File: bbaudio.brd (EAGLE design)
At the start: 88.9 x 127 mm, 35 parts, among them U1 V_REG_MIC2920, U2 V_REG_MIC2920, U3 LMZ14203

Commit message: Some more tewaks to the power section
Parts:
- removed C3: 1uF, rcl:C0603
- removed C4: 10uF, sparkfun:EIA3216
- removed U1: V_REG_MIC2920, sparkfun:SOT223
- added C10: 10uF, sparkfun:EIA3216
- added C7: 1uF, rcl:C0603
- added U4: VREG, nonolith:SOT23-3
- moved C6 16.1 mm to (62.2, 33.0), turned to 270 degrees
- moved C2 8.52 mm to (43.2, 29.2), turned to 90 degrees
- moved R3 7.73 mm to (67.3, 29.2), turned to 90 degrees
- moved R2 4.58 mm to (50.8, 25.4), turned to 0 degrees
- moved R4 2.84 mm to (64.8, 33.0)
- moved C9 2.84 mm to (64.8, 29.2), turned to 90 degrees
- moved C5 1.27 mm to (47.0, 33.0), turned to 270 degrees
- moved R1 1.27 mm to (50.8, 27.9), turned to 0 degrees
- moved U3 1.27 mm to (54.6, 39.4)
- moved C8 1.27 mm to (55.9, 27.9)
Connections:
- new net VCC: C2.A, U2.3
- net +12V: now also C1.1, U2.1
- net 1.8V: now also C7.1, U4.3; no longer C4.A, U1.3
- net 3.3V: now also C10.A, U4.2; no longer C2.A, C3.1, U1.1, U2.3
- net 5V: no longer C1.1, U2.1
- net GND: now also C10.C, C7.2, U4.1; no longer C3.2, C4.C, U1.2
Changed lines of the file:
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@@
 <element name="R8" library="SparkFun-Passives" package="0603-RES" value="56" x="41.91" y="71.12" rot="R180"/>
 <element name="R9" library="SparkFun-Passives" package="0603-RES" value="56" x="59.69" y="71.12" rot="R180"/>
-<element name="C3" library="rcl" package="C0603" value="1uF" x="26.67" y="31.75" rot="R180"/>
-<element name="C4" library="sparkfun" package="EIA3216" value="10uF" x="34.29" y="36.83" rot="R90"/>
-<element name="U1" library="sparkfun" package="SOT223" value="V_REG_MIC2920" x="27.94" y="38.1"/>
 <element name="C1" library="rcl" package="C0603" value="1uF" x="39.37" y="31.75" rot="R180"/>
-<element name="C2" library="sparkfun" package="EIA3216" value="10uF" x="46.99" y="36.83" rot="R270"/>
+<element name="C2" library="sparkfun" package="EIA3216" value="10uF" x="43.18" y="29.21" rot="R90"/>
 <element name="U2" library="sparkfun" package="SOT223" value="V_REG_MIC2920" x="40.64" y="38.1"/>
-<element name="U3" library="SparkFun-PowerIC" package="TO-PMOD-7" value="LMZ14203" x="55.88" y="39.37"/>
-<element name="C5" library="sparkfun" package="EIA3216" value="10uF" x="46.99" y="31.75"/>
-<element name="C6" library="sparkfun" package="EIA3216" value="100uF" x="46.99" y="27.94" rot="R180"/>
-<element name="R1" library="SparkFun-Passives" package="0603-RES" value="100K" x="52.07" y="27.94" rot="R90"/>
-<element name="R2" library="SparkFun-Passives" package="0603-RES" value="100K" x="54.61" y="27.94" rot="R90"/>
-<element name="C8" library="rcl" package="C0603" value="22pF" x="57.15" y="27.94" rot="R270"/>
-<element name="R3" library="SparkFun-Passives" package="0603-RES" value="5.62k" x="59.69" y="27.94" rot="R270"/>
-<element name="C9" library="rcl" package="C0603" value="22pF" x="62.23" y="27.94" rot="R270"/>
-<element name="R4" library="SparkFun-Passives" package="0603-RES" value="1.07k" x="62.23" y="31.75" rot="R270"/>
+<element name="U3" library="SparkFun-PowerIC" package="TO-PMOD-7" value="LMZ14203" x="54.61" y="39.37"/>
+<element name="C5" library="sparkfun" package="EIA3216" value="10uF" x="46.99" y="33.02" rot="R270"/>
+<element name="C6" library="sparkfun" package="EIA3216" value="100uF" x="62.23" y="33.02" rot="R270"/>
+<element name="R1" library="SparkFun-Passives" package="0603-RES" value="100K" x="50.8" y="27.94"/>
+<element name="R2" library="SparkFun-Passives" package="0603-RES" value="100K" x="50.8" y="25.4"/>
+<element name="C8" library="rcl" package="C0603" value="22pF" x="55.88" y="27.94" rot="R270"/>
+<element name="R3" library="SparkFun-Passives" package="0603-RES" value="5.62k" x="67.31" y="29.21" rot="R90"/>
+<element name="C9" library="rcl" package="C0603" value="22pF" x="64.77" y="29.21" rot="R90"/>
+<element name="R4" library="SparkFun-Passives" package="0603-RES" value="1.07k" x="64.77" y="33.02" rot="R270"/>
+<element name="C7" library="rcl" package="C0603" value="1uF" x="25.4" y="38.1" rot="R270"/>
+<element name="C10" library="sparkfun" package="EIA3216" value="10uF" x="29.21" y="34.29"/>
+<element name="U4" library="nonolith" package="SOT23-3" value="VREG" x="29.21" y="38.1" rot="R180"/>
 </elements>
 <signals>
@@
 <contactref element="U$1" pad="47"/>
 <contactref element="U$1" pad="48"/>
-<contactref element="C3" pad="2"/>
-<contactref element="C4" pad="C"/>
-<contactref element="U1" pad="2"/>
 <contactref element="C1" pad="2"/>
 <contactref element="C2" pad="C"/>
@@
 <vertex x="88.9" y="127"/>
 </polygon>
+<contactref element="C7" pad="2"/>
+<contactref element="C10" pad="C"/>
+<contactref element="U4" pad="1"/>
 </signal>
 <signal name="SYS_5V">
@@
 <contactref element="CLOCK_SPEED3" pad="3"/>
 <contactref element="S1" pad="C"/>
-<contactref element="C4" pad="A"/>
-<contactref element="U1" pad="3"/>
+<contactref element="C7" pad="1"/>
+<contactref element="U4" pad="3"/>
 <wire x1="46.99" y1="81.28" x2="74.87" y2="89.06" width="0" layer="19" extent="1-1"/>
 <wire x1="21.53" y1="89.06" x2="46.99" y2="81.28" width="0" layer="19" extent="1-1"/>
 <wire x1="74.87" y1="58.58" x2="74.87" y2="89.06" width="0" layer="19" extent="1-1"/>
 <wire x1="21.53" y1="58.58" x2="21.53" y2="89.06" width="0" layer="19" extent="1-1"/>
-<wire x1="34.29" y1="38.23" x2="21.53" y2="58.58" width="0" layer="19" extent="1-1"/>
-<wire x1="30.2514" y1="35.0012" x2="34.29" y2="38.23" width="0" layer="19" extent="1-1"/>
+<wire x1="25.4" y1="38.95" x2="21.53" y2="58.58" width="0" layer="19" extent="1-1"/>
+<wire x1="29.21" y1="39.4" x2="25.4" y2="38.95" width="0" layer="19" extent="1-1"/>
 </signal>
 <signal name="3.3V">
@@
 <contactref element="S2" pad="3"/>
 <contactref element="S3" pad="3"/>
-<contactref element="C3" pad="1"/>
-<contactref element="U1" pad="1"/>
-<contactref element="C2" pad="A"/>
-<contactref element="U2" pad="3"/>
+<contactref element="C10" pad="A"/>
+<contactref element="U4" pad="2"/>
 <wire x1="51.918" y1="71.12" x2="45.15" y2="95.02" width="0" layer="19" extent="1-1"/>
 <wire x1="55.6006" y1="60.2488" x2="51.918" y2="71.12" width="0" layer="19" extent="1-1"/>
 <wire x1="34.138" y1="71.12" x2="51.918" y2="71.12" width="0" layer="19" extent="1-1"/>
 <wire x1="37.8206" y1="60.2488" x2="34.138" y2="71.12" width="0" layer="19" extent="1-1"/>
-<wire x1="42.9514" y1="35.0012" x2="37.8206" y2="60.2488" width="0" layer="19" extent="1-1"/>
-<wire x1="46.99" y1="35.43" x2="42.9514" y2="35.0012" width="0" layer="19" extent="1-1"/>
-<wire x1="27.52" y1="31.75" x2="42.9514" y2="35.0012" width="0" layer="19" extent="1-1"/>
-<wire x1="25.6286" y1="35.0012" x2="27.52" y2="31.75" width="0" layer="19" extent="1-1"/>
-<wire x1="11.43" y1="51.435" x2="25.6286" y2="35.0012" width="0" layer="19" extent="1-1"/>
+<wire x1="30.16" y1="36.8" x2="37.8206" y2="60.2488" width="0" layer="19" extent="1-1"/>
+<wire x1="30.61" y1="34.29" x2="30.16" y2="36.8" width="0" layer="19" extent="1-1"/>
+<wire x1="11.43" y1="51.435" x2="30.16" y2="36.8" width="0" layer="19" extent="1-1"/>
 <wire x1="11.43" y1="53.975" x2="11.43" y2="51.435" width="0" layer="19" extent="1-1"/>
 </signal>
@@
 <contactref element="U$1" pad="52"/>
 <contactref element="U$1" pad="51"/>
-<contactref element="C1" pad="1"/>
-<contactref element="U2" pad="1"/>
 <contactref element="U3" pad="7"/>
 <contactref element="C6" pad="A"/>
 <contactref element="R3" pad="1"/>
 <contactref element="C9" pad="1"/>
-<wire x1="59.69" y1="28.79" x2="59.69" y2="31.74" width="0" layer="19" extent="1-1"/>
-<wire x1="62.23" y1="28.79" x2="59.69" y2="28.79" width="0" layer="19" extent="1-1"/>
-<wire x1="45.59" y1="27.94" x2="59.69" y2="28.79" width="0" layer="19" extent="1-1"/>
-<wire x1="40.22" y1="31.75" x2="45.59" y2="27.94" width="0" layer="19" extent="1-1"/>
-<wire x1="38.3286" y1="35.0012" x2="40.22" y2="31.75" width="0" layer="19" extent="1-1"/>
-<wire x1="13.97" y1="51.435" x2="38.3286" y2="35.0012" width="0" layer="19" extent="1-1"/>
+<wire x1="64.77" y1="28.36" x2="67.31" y2="28.36" width="0" layer="19" extent="1-1"/>
+<wire x1="62.23" y1="31.62" x2="64.77" y2="28.36" width="0" layer="19" extent="1-1"/>
+<wire x1="58.42" y1="31.74" x2="62.23" y2="31.62" width="0" layer="19" extent="1-1"/>
+<wire x1="13.97" y1="51.435" x2="58.42" y2="31.74" width="0" layer="19" extent="1-1"/>
 <wire x1="13.97" y1="53.975" x2="13.97" y2="51.435" width="0" layer="19" extent="1-1"/>
 </signal>
@@
 <contactref element="R1" pad="1"/>
 <contactref element="R2" pad="1"/>
-<wire x1="48.39" y1="31.75" x2="52.07" y2="31.74" width="0" layer="19" extent="1-1"/>
-<wire x1="52.07" y1="27.09" x2="52.07" y2="31.74" width="0" layer="19" extent="1-1"/>
-<wire x1="54.61" y1="27.09" x2="52.07" y2="27.09" width="0" layer="19" extent="1-1"/>
+<contactref element="C1" pad="1"/>
+<contactref element="U2" pad="1"/>
+<wire x1="46.99" y1="31.62" x2="50.8" y2="31.74" width="0" layer="19" extent="1-1"/>
+<wire x1="49.95" y1="27.94" x2="50.8" y2="31.74" width="0" layer="19" extent="1-1"/>
+<wire x1="49.95" y1="25.4" x2="49.95" y2="27.94" width="0" layer="19" extent="1-1"/>
+<wire x1="40.22" y1="31.75" x2="46.99" y2="31.62" width="0" layer="19" extent="1-1"/>
+<wire x1="38.3286" y1="35.0012" x2="40.22" y2="31.75" width="0" layer="19" extent="1-1"/>
 </signal>
 <signal name="N$6">
 <contactref element="U3" pad="2"/>
 <contactref element="R1" pad="2"/>
-<wire x1="52.07" y1="28.79" x2="53.34" y2="31.74" width="0" layer="19" extent="1-1"/>
+<wire x1="51.65" y1="27.94" x2="52.07" y2="31.74" width="0" layer="19" extent="1-1"/>
 </signal>
 <signal name="N$7">
 <contactref element="U3" pad="3"/>
 <contactref element="R2" pad="2"/>
-<wire x1="54.61" y1="28.79" x2="54.61" y2="31.74" width="0" layer="19" extent="1-1"/>
+<wire x1="51.65" y1="25.4" x2="53.34" y2="31.74" width="0" layer="19" extent="1-1"/>
 </signal>
 <signal name="N$8">
 <contactref element="U3" pad="5"/>
 <contactref element="C8" pad="1"/>
-<wire x1="57.15" y1="28.79" x2="57.15" y2="31.74" width="0" layer="19" extent="1-1"/>
+<wire x1="55.88" y1="28.79" x2="55.88" y2="31.74" width="0" layer="19" extent="1-1"/>
 </signal>
 <signal name="N$13">
@@
 <contactref element="C9" pad="2"/>
 <contactref element="R4" pad="2"/>
-<wire x1="62.23" y1="27.09" x2="62.23" y2="30.9" width="0" layer="19" extent="1-1"/>
-<wire x1="59.69" y1="27.09" x2="62.23" y2="27.09" width="0" layer="19" extent="1-1"/>
-<wire x1="58.45" y1="31.74" x2="62.23" y2="30.9" width="0" layer="19" extent="1-1"/>
+<wire x1="64.77" y1="30.06" x2="67.31" y2="30.06" width="0" layer="19" extent="1-1"/>
+<wire x1="64.77" y1="32.17" x2="64.77" y2="30.06" width="0" layer="19" extent="1-1"/>
+<wire x1="57.18" y1="31.74" x2="64.77" y2="32.17" width="0" layer="19" extent="1-1"/>
+</signal>
+<signal name="VCC">
+<contactref element="C2" pad="A"/>
+<contactref element="U2" pad="3"/>
+<wire x1="42.9514" y1="35.0012" x2="43.18" y2="30.61" width="0" layer="19" extent="1-1"/>
 </signal>
 </signals>

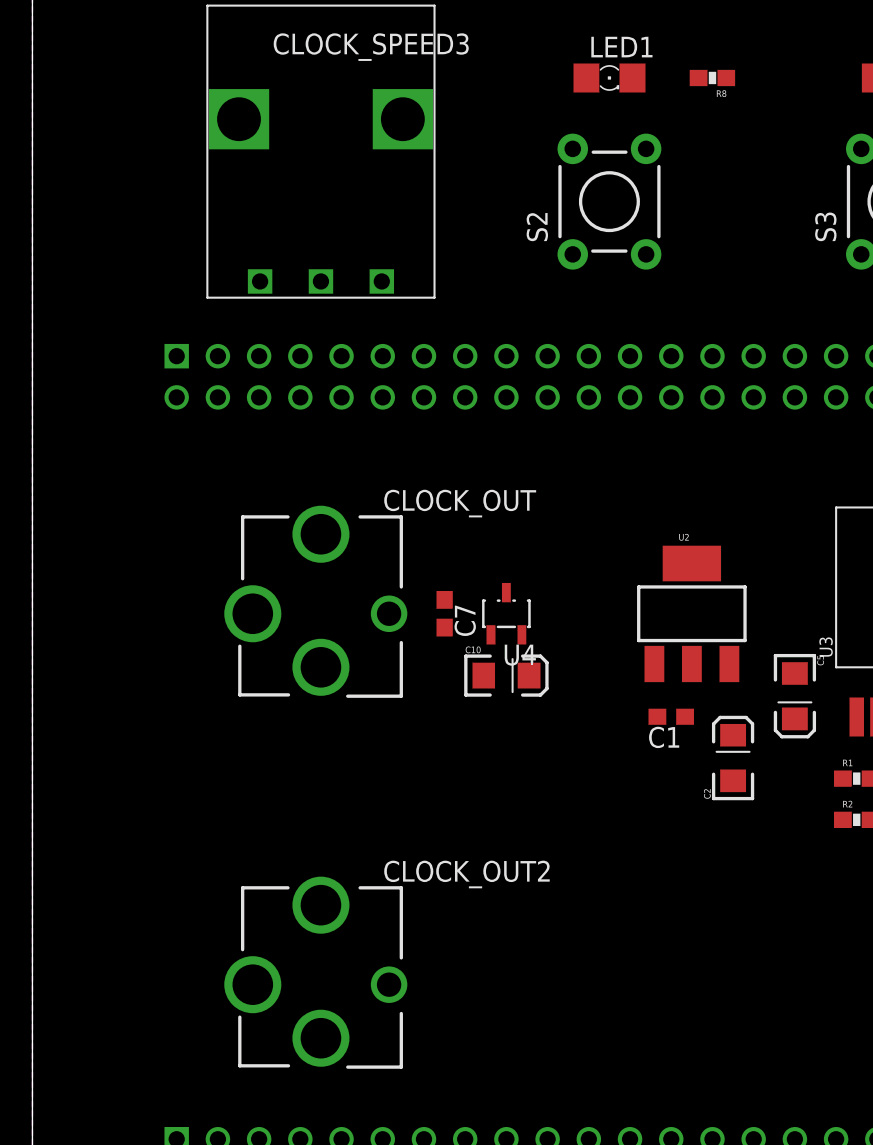
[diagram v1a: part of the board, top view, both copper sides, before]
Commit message: Added codec and power connector
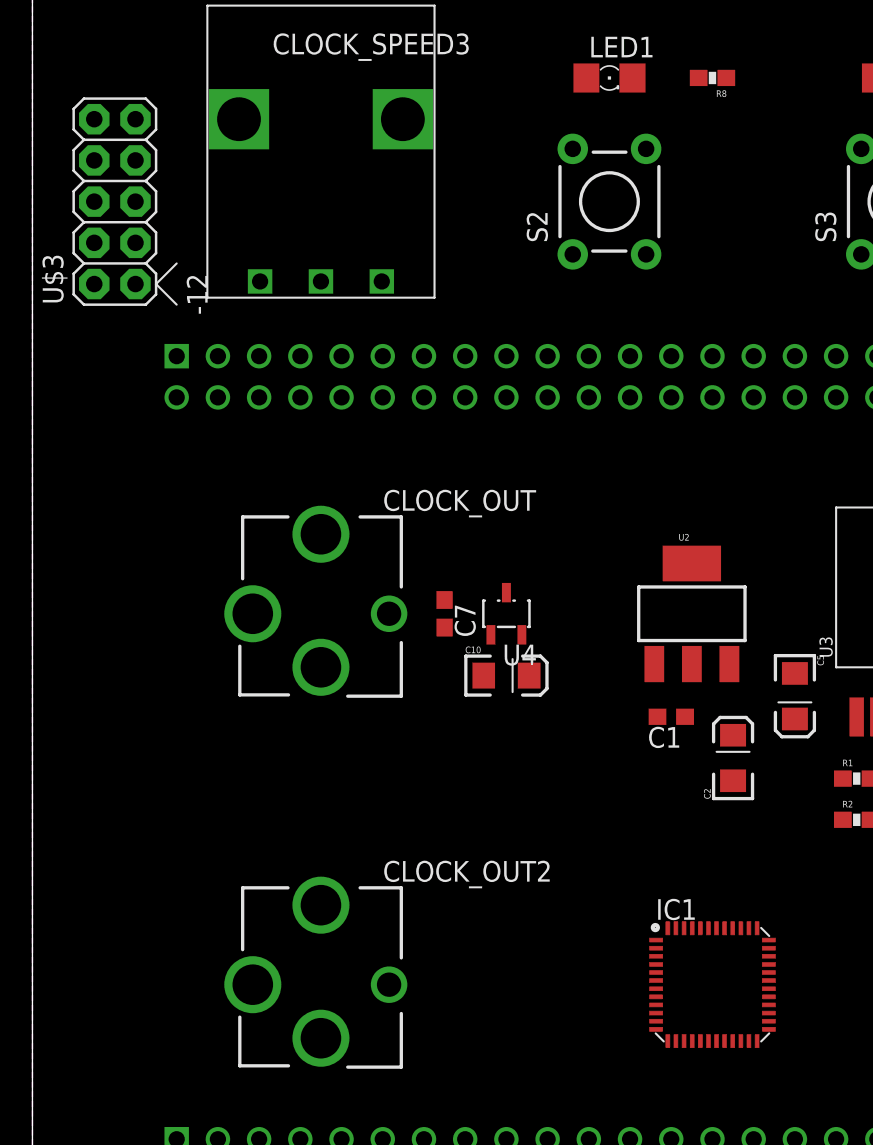
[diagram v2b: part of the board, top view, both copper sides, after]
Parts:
- added IC1: TLV320AIC3106, codec:QFN48
- added U$3: POWER_SIMPLE10, eurorack:POWER_10
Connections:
- new net -12V: U$3.1, U$3.2
- net +12V: now also U$3.10, U$3.9
- net GND: now also U$3.3, U$3.4, U$3.5, U$3.6, U$3.7, U$3.8
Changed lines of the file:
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@@
 <element name="C10" library="sparkfun" package="EIA3216" value="10uF" x="29.21" y="34.29"/>
 <element name="U4" library="nonolith" package="SOT23-3" value="VREG" x="29.21" y="38.1" rot="R180"/>
+<element name="IC1" library="codec" package="QFN48" value="TLV320AIC3106" x="41.91" y="15.24"/>
+<element name="U$3" library="eurorack" package="POWER_10" value="POWER_SIMPLE10" x="5.08" y="63.5" rot="R90"/>
 </elements>
 <signals>
@@
 <contactref element="C10" pad="C"/>
 <contactref element="U4" pad="1"/>
+<contactref element="U$3" pad="5"/>
+<contactref element="U$3" pad="4"/>
+<contactref element="U$3" pad="8"/>
+<contactref element="U$3" pad="7"/>
+<contactref element="U$3" pad="3"/>
+<contactref element="U$3" pad="6"/>
 </signal>
 <signal name="SYS_5V">
@@
 <contactref element="C1" pad="1"/>
 <contactref element="U2" pad="1"/>
+<contactref element="U$3" pad="10"/>
+<contactref element="U$3" pad="9"/>
 <wire x1="46.99" y1="31.62" x2="50.8" y2="31.74" width="0" layer="19" extent="1-1"/>
 <wire x1="49.95" y1="27.94" x2="50.8" y2="31.74" width="0" layer="19" extent="1-1"/>
@@
 <wire x1="40.22" y1="31.75" x2="46.99" y2="31.62" width="0" layer="19" extent="1-1"/>
 <wire x1="38.3286" y1="35.0012" x2="40.22" y2="31.75" width="0" layer="19" extent="1-1"/>
+<wire x1="6.35" y1="68.58" x2="38.3286" y2="35.0012" width="0" layer="19" extent="1-1"/>
+<wire x1="3.81" y1="68.58" x2="6.35" y2="68.58" width="0" layer="19" extent="1-1"/>
 </signal>
 <signal name="N$6">
@@
 <wire x1="42.9514" y1="35.0012" x2="43.18" y2="30.61" width="0" layer="19" extent="1-1"/>
 </signal>
+<signal name="-12V">
+<contactref element="U$3" pad="1"/>
+<contactref element="U$3" pad="2"/>
+<wire x1="3.81" y1="58.42" x2="6.35" y2="58.42" width="0" layer="19" extent="1-1"/>
+</signal>
 </signals>

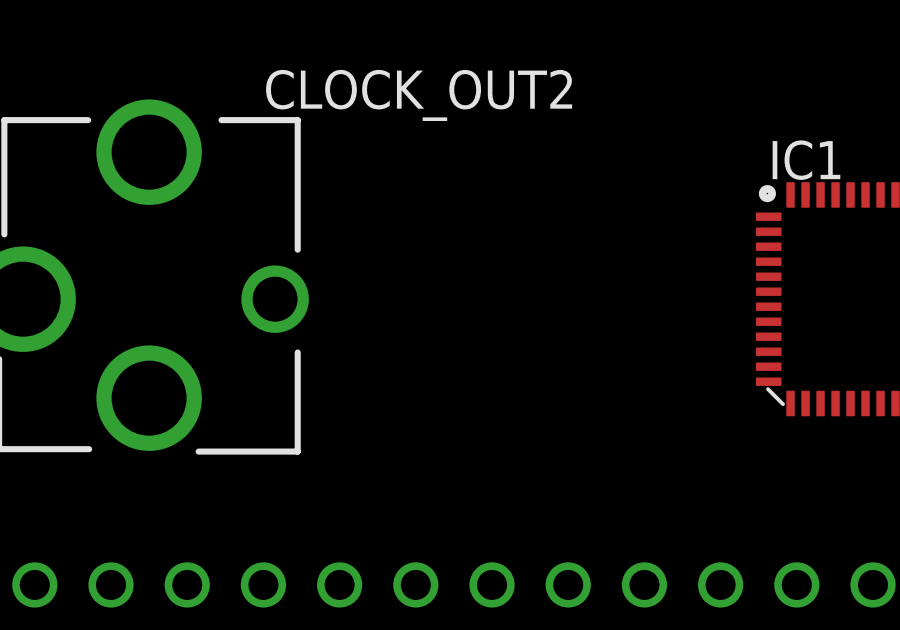
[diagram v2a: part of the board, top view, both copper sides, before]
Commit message: Added clock source
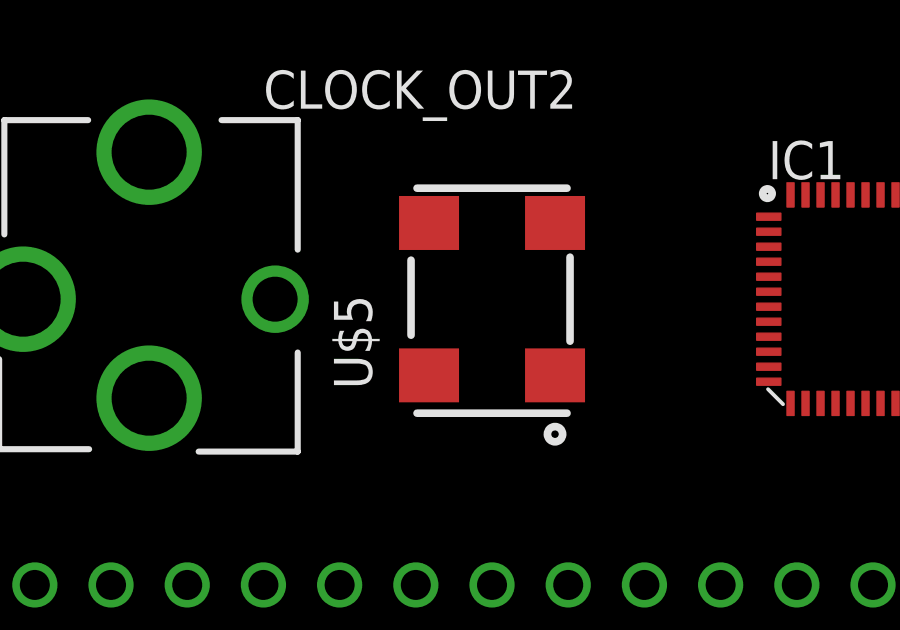
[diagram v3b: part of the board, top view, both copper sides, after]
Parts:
- added U$5: FXO_HC73, codec:4PIN
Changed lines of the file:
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@@
 <element name="IC1" library="codec" package="QFN48" value="TLV320AIC3106" x="41.91" y="15.24"/>
 <element name="U$3" library="eurorack" package="POWER_10" value="POWER_SIMPLE10" x="5.08" y="63.5" rot="R90"/>
+<element name="U$5" library="codec" package="4PIN" value="FXO_HC73" x="29.21" y="15.24" rot="R90"/>
 </elements>
 <signals>
